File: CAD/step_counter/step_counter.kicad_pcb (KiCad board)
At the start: 2 copper layers, 80 x 40 mm, 60 parts, among them J1 Conn_01x14_Pin, U1 74HC161, U2 74HC109, U3 74HC109, U4 74HC08, U5 74HC08, U6 74HC02, U7 74HC02, U8 74HC04

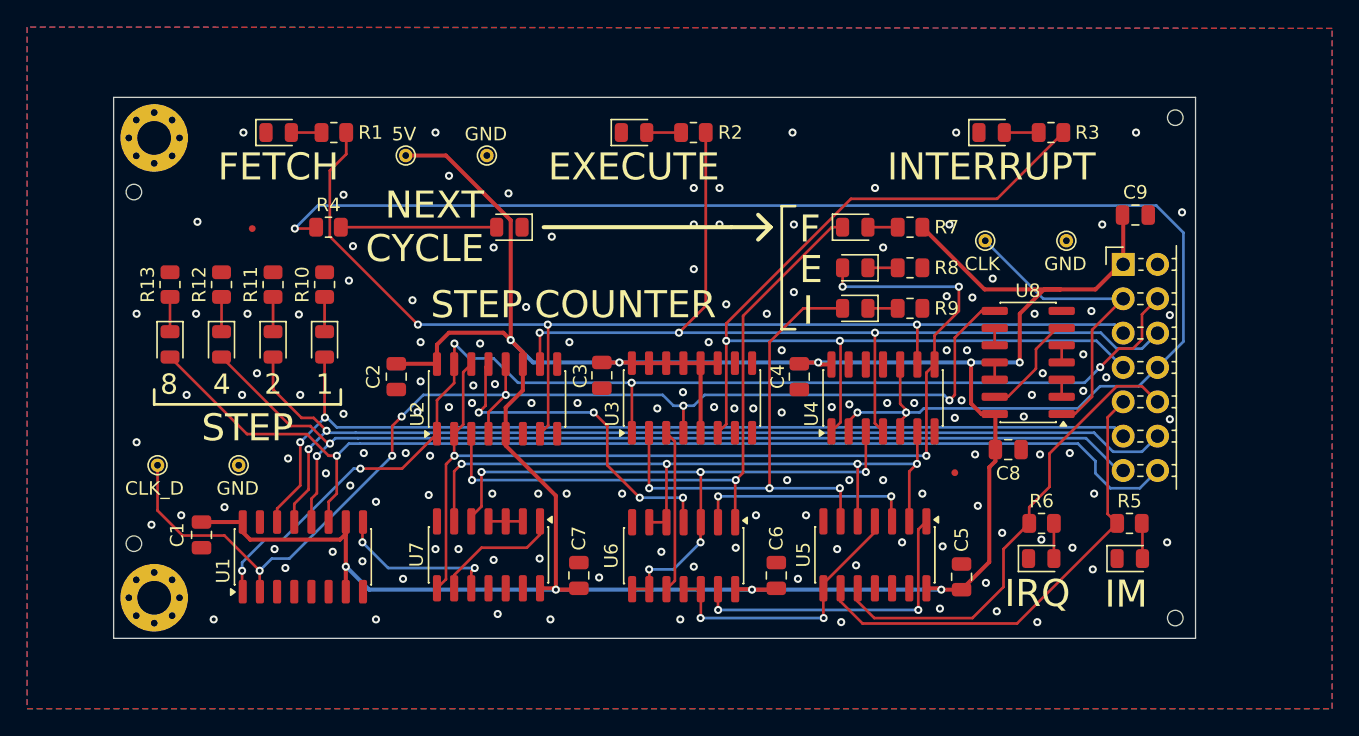
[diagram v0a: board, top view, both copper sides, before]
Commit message: update Step Counter, more ground planes
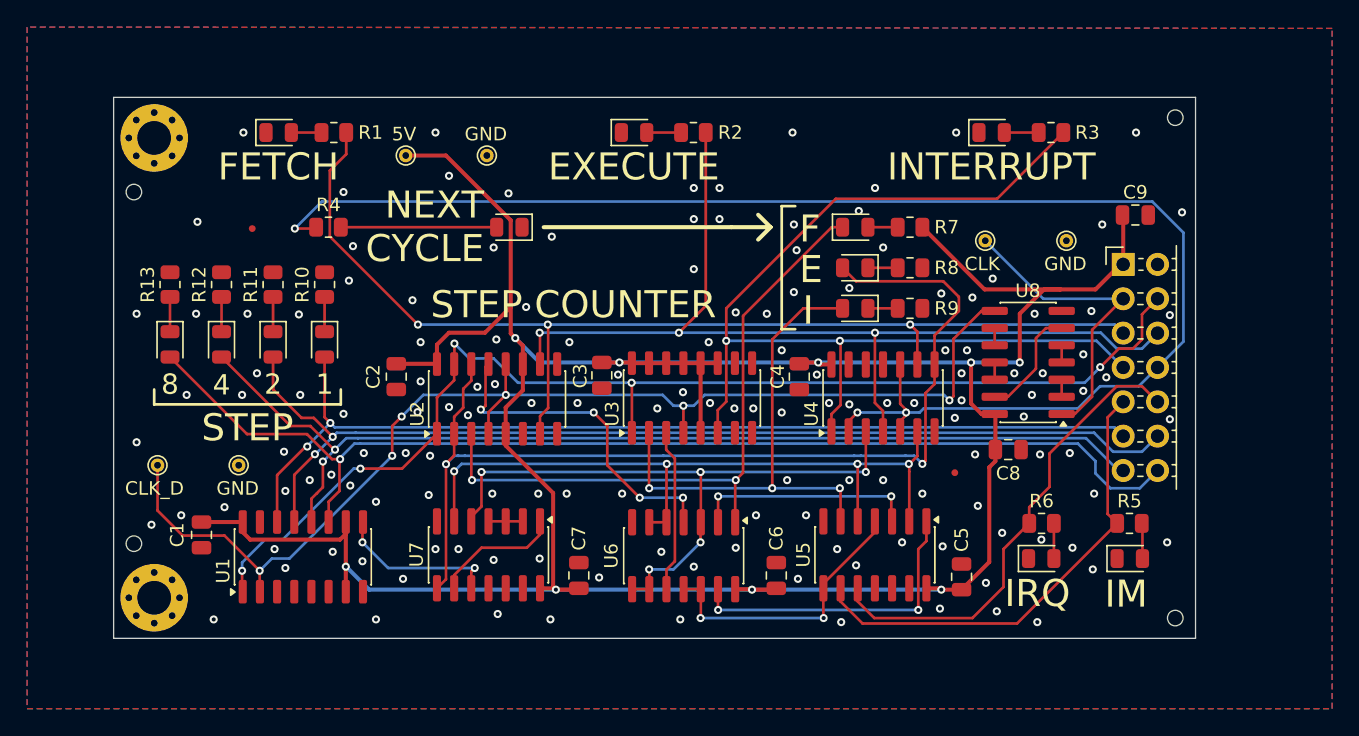
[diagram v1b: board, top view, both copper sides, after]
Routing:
- net INTERRUPT: track 76.4 -> 77.1 mm
- net /end_execute: track 54.9 -> 54.4 mm
- net /end_fetch: track 76.3 -> 76.5 mm, vias 4 -> 2
- net GND: vias 138 -> 146

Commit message: step counter - layout improvements
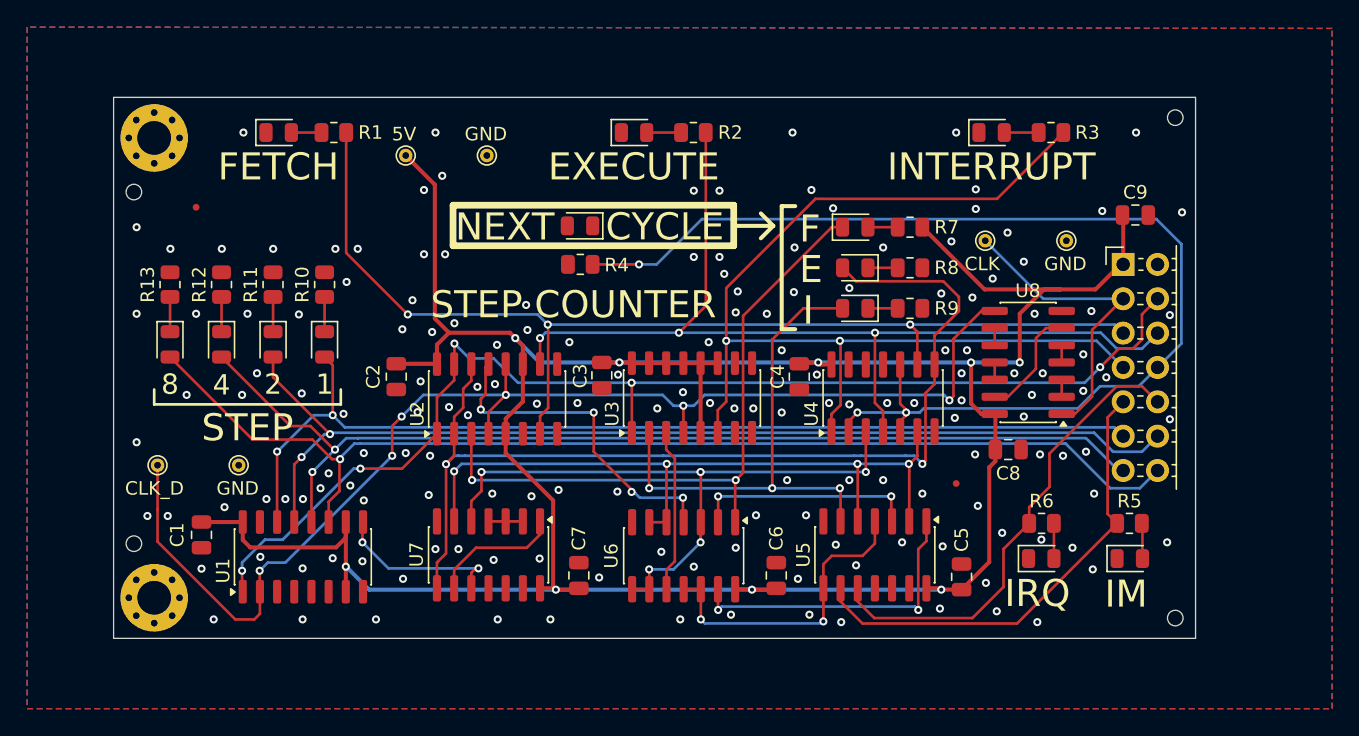
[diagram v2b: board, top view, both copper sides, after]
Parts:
- moved R4 18.8 mm to (93.1, 66.0), turned to 180 degrees
- moved D4 5.23 mm to (93.1, 63.2)
- moved FID1 4.44 mm to (64.7, 61.8)
- moved FID2 0.81 mm to (120.9, 82.2)
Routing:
- net cycle_end: track 110.4 -> 84.5 mm
- net Net-(D4-A): track 11.5 -> 0.00 mm
- net +5V: track 224.1 -> 219.3 mm
- net clk_d: track 89.1 -> 93.7 mm
- net /int: track 21.2 -> 23.1 mm
- net FETCH: track 81.2 -> 80.2 mm
- net /step.0: track 73.1 -> 74.1 mm
- net INTERRUPT: track 77.1 -> 77.8 mm
- net /step.3: track 84.1 -> 83.6 mm
- net GND: vias 146 -> 163
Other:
- board text added: "CYCLE"
- board text added: "NEXT"
- board text removed: "NEXT CYCLE"

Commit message: update KiCAD version 10.0
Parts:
- removed G***: LOGO, 8-bit_computer:qr-code-github

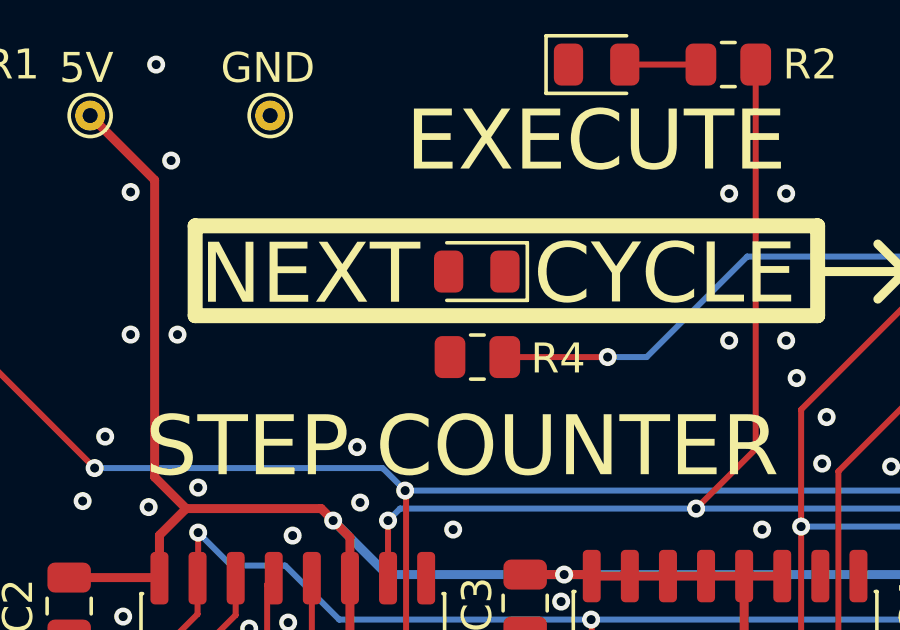
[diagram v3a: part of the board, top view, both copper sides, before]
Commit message: exclude known warnings in ERC and DRC
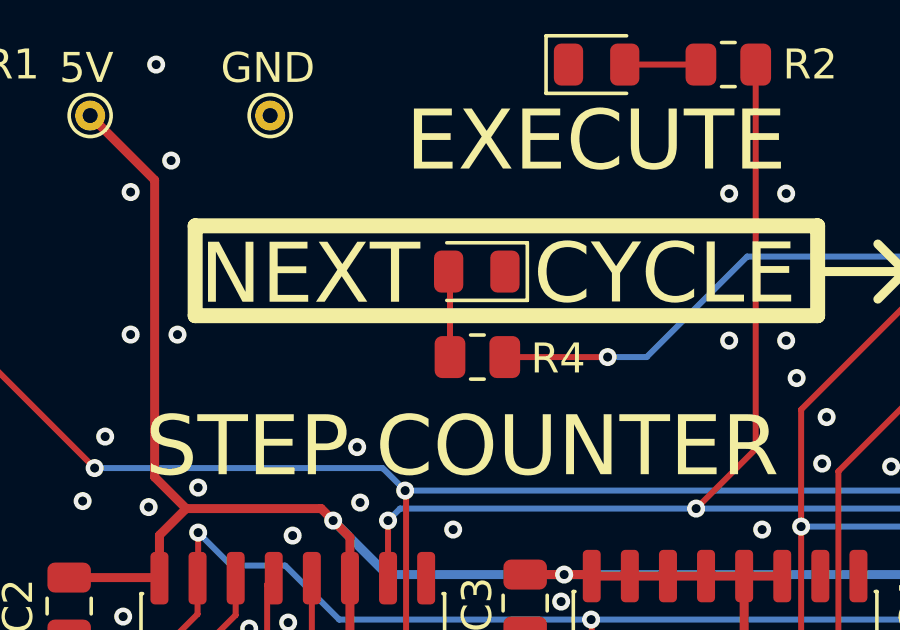
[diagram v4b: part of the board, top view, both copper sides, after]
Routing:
- net Net-(D4-A): track 0.00 -> 2.80 mm
